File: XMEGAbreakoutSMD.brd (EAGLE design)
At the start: 160 x 100 mm, 22 parts, among them IC1 XMEGA16A4A

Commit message: smd breakout finished
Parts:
- added JUMPER1, JUMPER2: 0, fab:R1206FAB
- IC1: value XMEGA16A4A -> XMEGA16A4; device atmel:TQFP44 -> atmel:TQFP44-FAB
- moved D5 103.8 mm to (96.2, 23.2)
- moved D4 100.7 mm to (96.2, 21.0)
- moved D3 93.3 mm to (83.8, 34.0), turned to 40 degrees
- moved D1 93.2 mm to (91.4, 27.9), turned to 180 degrees
- moved D2 93.0 mm to (90.2, 25.7), turned to 180 degrees
- moved C4 55.6 mm to (100.4, 40.8)
- moved R3 55.3 mm to (100.2, 37.8)
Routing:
- net RESET: track 47.8 -> 182.6 mm
- net VBUS: track 4.82 -> 99.9 mm
- net N$25: track 0.00 -> 44.7 mm
- net GND: track 121.3 -> 158.3 mm, vias 6 -> 8
- net D+: track 20.1 -> 37.3 mm
- net D-: track 24.8 -> 38.9 mm
- net PE2: track 46.3 -> 42.0 mm
- net PE3: track 47.9 -> 44.2 mm
- net VCC: track 64.0 -> 61.3 mm
- net MOSI: track 36.4 -> 35.3 mm

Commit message: eagle layout finished
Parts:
- moved C2 17.6 mm to (58.3, 47.1)
- moved C1 11.6 mm to (53.7, 47.8), turned to 270 degrees
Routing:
- net VCC: track 61.3 -> 56.0 mm
- net GND: track 158.3 -> 156.0 mm
- net RESET: track 182.6 -> 181.5 mm

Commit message: final output pngs
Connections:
- net GND: now also IC2.1; no longer IC2.2
- net VBUS: now also IC2.3; no longer IC2.1
- net VCC: now also IC2.2; no longer IC2.3
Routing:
- net VBUS: track 99.9 -> 107.4 mm
- net GND: track 156.0 -> 163.4 mm, vias 8 -> 9
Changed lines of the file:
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@@
 <signal name="VBUS">
 <contactref element="U$1" pad="VBUS"/>
-<contactref element="IC2" pad="1"/>
+<contactref element="IC2" pad="3"/>
 <contactref element="R2" pad="2"/>
-<wire x1="49.765921875" y1="47.79394375" x2="49.76418125" y2="47.795684375" width="0.6096" layer="1"/>
 <contactref element="D1" pad="CATHODE"/>
 <contactref element="D2" pad="CATHODE"/>
@@
 <wire x1="93.14" y1="27.94" x2="93.14" y2="26.9875" width="0.6096" layer="1"/>
 <wire x1="93.14" y1="26.9875" x2="91.87" y2="25.7175" width="0.6096" layer="1"/>
-<wire x1="49.76418125" y1="47.795684375" x2="49.76418125" y2="43.737496875" width="0.6096" layer="1"/>
-<wire x1="49.76418125" y1="43.737496875" x2="49.229021875" y2="43.2023375" width="0.6096" layer="1"/>
 <wire x1="91.87" y1="25.7175" x2="92.075" y2="25.7175" width="0.6096" layer="1"/>
 <wire x1="92.075" y1="25.7175" x2="94.615" y2="23.1775" width="0.6096" layer="1"/>
@@
 <wire x1="96.341234375" y1="28.42404375" x2="93.62404375" y2="28.42404375" width="0.3048" layer="1"/>
 <wire x1="93.62404375" y1="28.42404375" x2="93.14" y2="27.94" width="0.3048" layer="1"/>
+<wire x1="49.229021875" y1="43.2023375" x2="49.229021875" y2="44.115978125" width="0.6096" layer="1"/>
+<wire x1="49.229021875" y1="44.115978125" x2="46.99" y2="46.355" width="0.6096" layer="1"/>
+<wire x1="46.99" y1="46.355" x2="46.99" y2="51.435" width="0.6096" layer="1"/>
+<wire x1="46.99" y1="51.435" x2="47.625" y2="52.07" width="0.6096" layer="1"/>
+<wire x1="49.76418125" y1="52.395684375" x2="47.950684375" y2="52.395684375" width="0.6096" layer="1"/>
+<wire x1="47.950684375" y1="52.395684375" x2="47.625" y2="52.07" width="0.6096" layer="1"/>
 </signal>
 <signal name="D+">
@@
 <contactref element="C1" pad="2"/>
 <contactref element="IC2" pad="4"/>
-<contactref element="IC2" pad="2"/>
+<contactref element="IC2" pad="1"/>
 <contactref element="LED1" pad="C"/>
-<wire x1="43.46418125" y1="50.095684375" x2="49.76418125" y2="50.095684375" width="0.6096" layer="1"/>
 <wire x1="80.9121625" y1="49.23378125" x2="80.8930125" y2="49.21463125" width="0.6096" layer="1"/>
 <wire x1="86.880465625" y1="46.40535" x2="86.880465625" y2="49.21463125" width="0.6096" layer="1"/>
@@
 <wire x1="43.46418125" y1="50.095684375" x2="43.46418125" y2="44.901234375" width="0.6096" layer="1"/>
 <wire x1="43.46418125" y1="44.901234375" x2="43.624790625" y2="44.740625" width="0.6096" layer="1"/>
-<wire x1="49.76418125" y1="50.095684375" x2="51.162003125" y2="50.095684375" width="0.6096" layer="1"/>
-<wire x1="51.162003125" y1="50.095684375" x2="51.65624375" y2="49.76019375" width="0.6096" layer="1"/>
-<wire x1="51.65624375" y1="49.76019375" x2="51.566828125" y2="46.368265625" width="0.6096" layer="1"/>
 <via x="51.5176125" y="44.501325" extent="1-16" drill="0.1" diameter="1.016"/>
 <wire x1="51.566828125" y1="46.368265625" x2="51.5176125" y2="44.501325" width="0.6096" layer="1"/>
@@
 <wire x1="53.68453125" y1="46.439421875" x2="51.637984375" y2="46.439421875" width="0.6096" layer="1"/>
 <wire x1="51.637984375" y1="46.439421875" x2="51.566828125" y2="46.368265625" width="0.6096" layer="1"/>
+<wire x1="49.76418125" y1="47.795684375" x2="50.139409375" y2="47.795684375" width="0.6096" layer="1"/>
+<wire x1="50.139409375" y1="47.795684375" x2="51.566828125" y2="46.368265625" width="0.6096" layer="1"/>
+<wire x1="43.46418125" y1="50.095684375" x2="43.46418125" y2="53.62418125" width="0.6096" layer="1"/>
+<wire x1="43.46418125" y1="53.62418125" x2="43.815" y2="53.975" width="0.6096" layer="1"/>
+<via x="43.815" y="53.975" extent="1-16" drill="0.0254" diameter="1.016"/>
+<wire x1="43.815" y1="53.975" x2="43.815" y2="52.2039375" width="0.6096" layer="16"/>
+<wire x1="43.815" y1="52.2039375" x2="51.5176125" y2="44.501325" width="0.6096" layer="16"/>
 </signal>
 <signal name="VCC">
@@
 <contactref element="R1" pad="1"/>
 <contactref element="C2" pad="1"/>
-<contactref element="IC2" pad="3"/>
+<contactref element="IC2" pad="2"/>
 <contactref element="C1" pad="1"/>
-<wire x1="49.780315625" y1="52.41181875" x2="49.76418125" y2="52.395684375" width="0.6096" layer="1"/>
 <wire x1="83.37896875" y1="50.9116875" x2="83.484503125" y2="51.017221875" width="0.4064" layer="1"/>
-<wire x1="49.76418125" y1="52.395684375" x2="51.69043125" y2="52.395684375" width="0.6096" layer="1"/>
-<wire x1="51.69043125" y1="52.395684375" x2="54.583059375" y2="49.50305625" width="0.6096" layer="1"/>
 <wire x1="54.583059375" y1="49.50305625" x2="54.871484375" y2="49.21463125" width="0.6096" layer="1"/>
 <wire x1="54.871484375" y1="49.21463125" x2="59.69" y2="49.21463125" width="0.6096" layer="1"/>
@@
 <wire x1="53.68453125" y1="49.239421875" x2="54.319425" y2="49.239421875" width="0.6096" layer="1"/>
 <wire x1="54.319425" y1="49.239421875" x2="54.583059375" y2="49.50305625" width="0.6096" layer="1"/>
+<wire x1="54.583059375" y1="49.50305625" x2="53.34" y2="49.50305625" width="0.4064" layer="1"/>
+<wire x1="53.34" y1="49.50305625" x2="53.34" y2="48.895" width="0.4064" layer="1"/>
+<wire x1="49.76418125" y1="50.095684375" x2="52.139315625" y2="50.095684375" width="0.6096" layer="1"/>
+<wire x1="52.139315625" y1="50.095684375" x2="53.34" y2="48.895" width="0.6096" layer="1"/>
 <wire x1="70.83015" y1="39.2389" x2="70.83015" y2="39.217409375" width="0" layer="19" extent="1-1"/>
 </signal>

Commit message: small changes
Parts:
- added C5: 4.7uF, fab:C1206
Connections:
- net GND: now also C5.2
- net VBUS: now also C5.1
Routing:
- net VBUS: track 107.4 -> 110.5 mm
- net GND: track 163.4 -> 165.4 mm

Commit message: final
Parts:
- removed D1, D2, D3, D4, D5: (no value), fab:SOD123
- added U$2: INVERTER, SparkFun:SOT23-5
- JP1: device SparkFun:1X08_SMD_ALT_2X1X4 -> SparkFun:1X08_2X1X4
- JP2, JP3, JP5: device SparkFun:1X08_SMD_ALT -> SparkFun:1X08
- moved JP1 20.4 mm to (69.8, 62.2), turned to 0 degrees
- turned JP2 to 180 degrees
- turned JP3 to 180 degrees
- turned JP5 to 0 degrees
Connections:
- net D+: now also U$2.3; no longer D2.ANODE, D3.CATHODE
- net D-: now also U$2.4; no longer D1.ANODE, D4.CATHODE
- net GND: now also U$2.2
- net N$25: no longer D3.ANODE, D4.ANODE, D5.ANODE
- net VBUS: now also U$2.5; no longer D1.CATHODE, D2.CATHODE, D5.CATHODE
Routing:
- net N$25: track 44.7 -> 28.8 mm
- net GND: track 165.4 -> 175.9 mm, vias 9 -> 10
- net D-: track 38.9 -> 32.2 mm
- net VBUS: track 110.5 -> 107.0 mm
- net D+: track 37.3 -> 40.8 mm
- net PA4: track 13.7 -> 17.0 mm
- net PE0: track 46.0 -> 47.8 mm
- net PA7: track 21.8 -> 20.2 mm
- net PE3: track 44.2 -> 42.6 mm
- net N$15: track 37.6 -> 35.9 mm
- net N$13: track 34.6 -> 33.0 mm
- net PA5: track 17.1 -> 15.4 mm
- net N$9: track 30.3 -> 28.7 mm
- net N$11: track 25.9 -> 24.3 mm
- net N$24: track 17.4 -> 19.0 mm
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
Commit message: reorganizing
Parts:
- JP1: device SparkFun:1X08_2X1X4 -> SparkFun:1X08_SMD_ALT_2X1X4
- JP2, JP3, JP5: device SparkFun:1X08 -> SparkFun:1X08_SMD_ALT
- moved JP1 20.4 mm to (90.2, 62.2), turned to 180 degrees
- turned JP2 to 0 degrees
- turned JP3 to 0 degrees
- turned JP5 to 180 degrees
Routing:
- net PA4: track 17.0 -> 13.7 mm
- net VBUS: track 107.0 -> 109.4 mm
- net N$13: track 33.0 -> 34.6 mm
- net SCK: track 27.1 -> 28.7 mm
- net N$24: track 19.0 -> 17.4 mm
- net N$12: track 31.9 -> 30.2 mm
- net MOSI: track 33.6 -> 35.3 mm
- net MISO: track 29.6 -> 28.0 mm
- net D+: track 40.8 -> 39.1 mm
- net N$18: track 22.2 -> 20.6 mm
- net N$14: track 33.0 -> 31.3 mm
- net N$7: track 15.3 -> 17.0 mm
- net N$8: track 15.5 -> 13.9 mm
- net N$5: track 14.9 -> 16.5 mm
- net D-: track 32.2 -> 33.8 mm
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
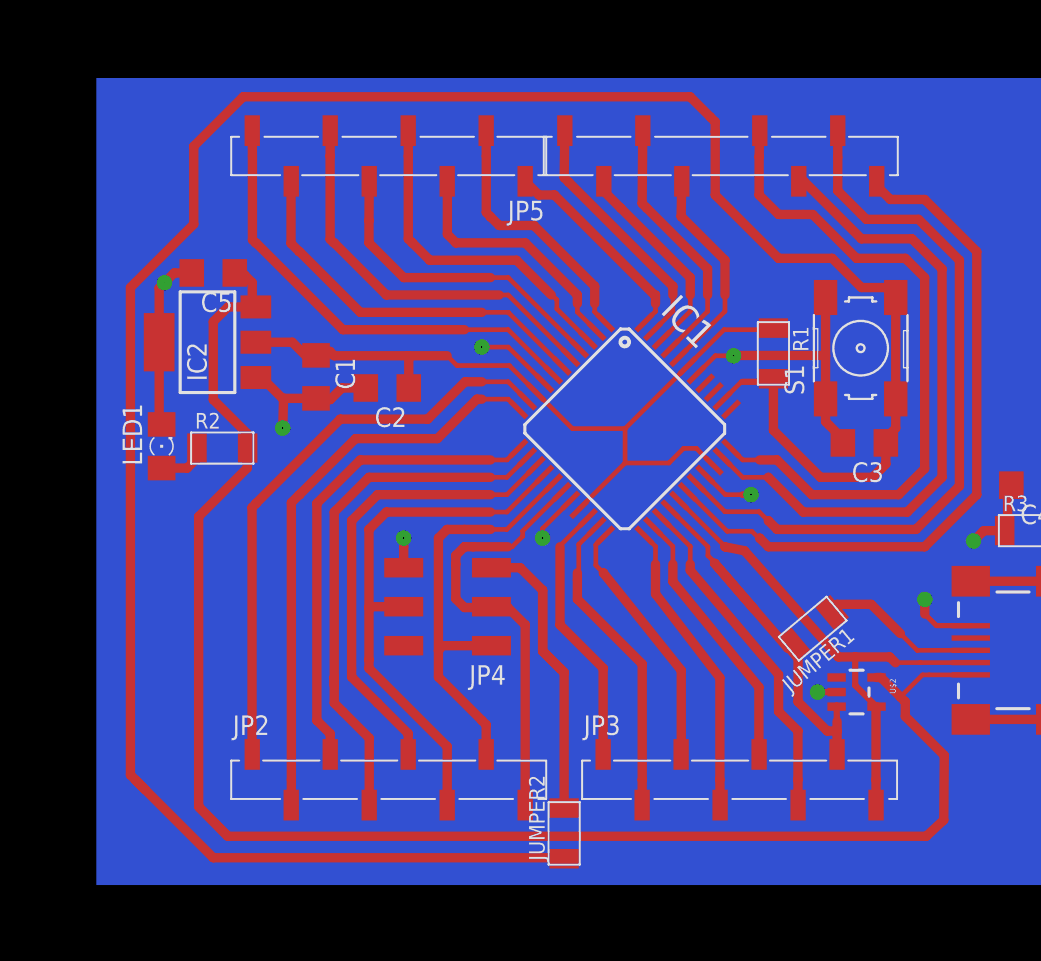
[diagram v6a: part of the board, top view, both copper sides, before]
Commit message: power pins broken out
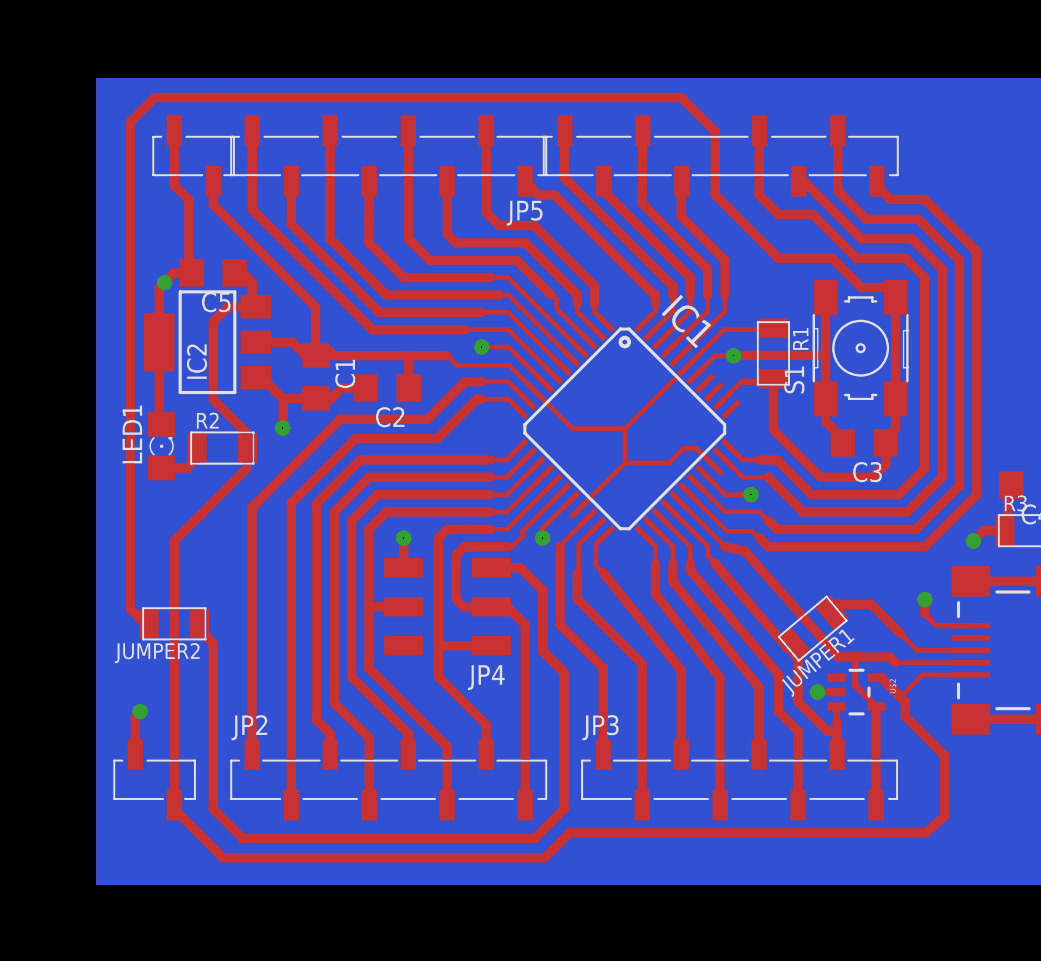
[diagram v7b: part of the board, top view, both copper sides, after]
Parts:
- added JP8, JP9: (no value), SparkFun:1X02_SMD_STRAIGHT_ALT
- moved JUMPER2 28.8 mm to (44.5, 31.8), turned to 180 degrees
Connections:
- net GND: now also JP8.1, JP9.1
- net VBUS: now also JP9.2
- net VCC: now also JP8.2
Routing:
- net GND: track 175.9 -> 218.0 mm, vias 10 -> 11
- net VCC: track 55.9 -> 70.0 mm
- net VBUS: track 109.4 -> 111.5 mm
- net RESET: track 181.4 -> 180.5 mm
- net N$10: track 25.0 -> 24.3 mm
- net N$9: track 30.3 -> 30.9 mm

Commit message: latest
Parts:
- added JP6: (no value), fab:2X03SMD
- moved C3 13.5 mm to (91.2, 57.0), turned to 90 degrees
- moved JP1 10.2 mm to (100.4, 62.2)
- moved C4 1.73 mm to (101.7, 41.9), turned to 90 degrees
- moved S1 0.95 mm to (88.2, 49.7)
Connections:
- new net DAT: IC1.34, JP6.1
- net GND: now also JP6.6
- net RESET: now also JP6.5; no longer JP4.5
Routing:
- net RESET: track 180.5 -> 117.7 mm
- net DAT: track 0.00 -> 43.9 mm
- net GND: track 218.0 -> 246.7 mm, vias 11 -> 12
- net PE3: track 44.2 -> 37.6 mm
- net PE2: track 42.2 -> 36.9 mm
- net PE1: track 48.0 -> 43.6 mm
- net PE0: track 45.9 -> 43.7 mm
- net VBUS: track 111.5 -> 109.3 mm
